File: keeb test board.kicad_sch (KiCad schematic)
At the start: 15 parts, among them SW12 SW_Push, SW14 SW_Push, SW15 SW_Push, SW3 SW_Push, SW6 SW_Push, SW9 SW_Push, U1 BluePill_V1.1

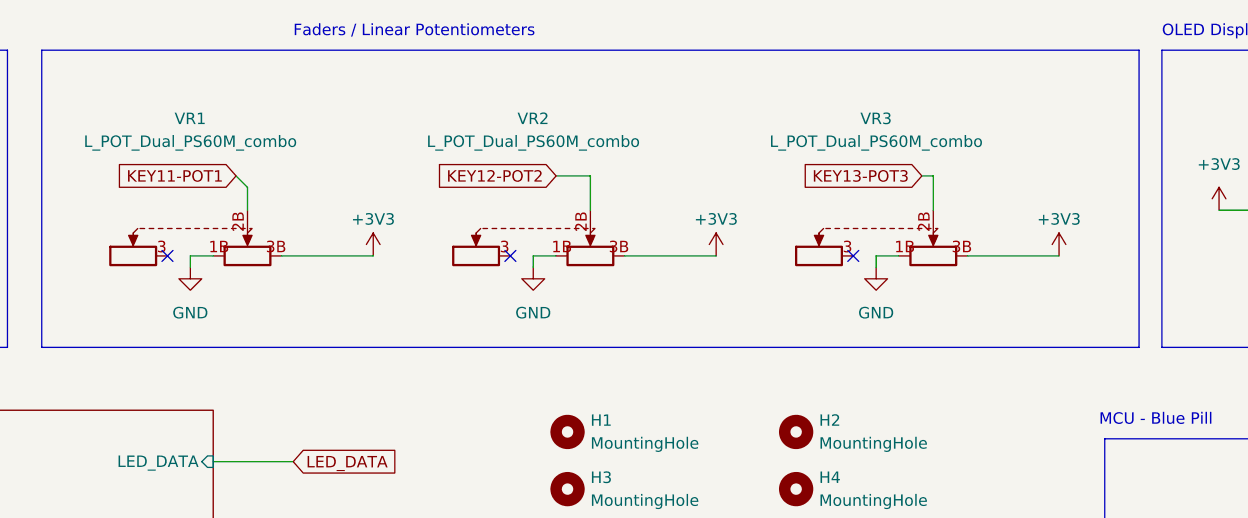
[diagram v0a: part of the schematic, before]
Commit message: LED pins fixed, lots of rerouting
Corrected LED and routed accordingly. Lots of other misc, changes to improve routing.
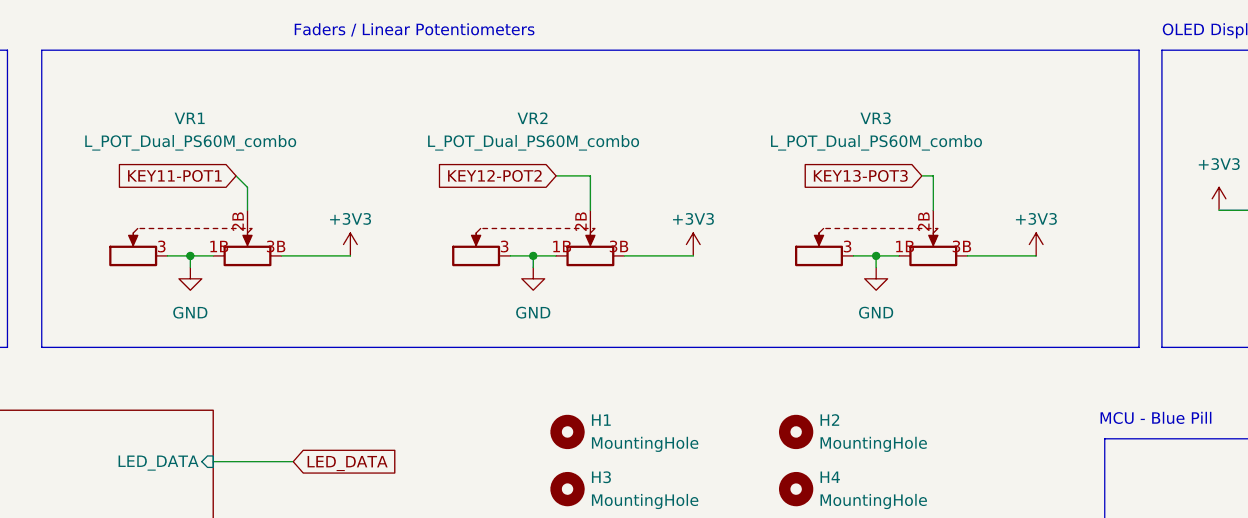
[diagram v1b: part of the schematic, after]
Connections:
- net GND: now also VR1.3, VR2.3, VR3.3
- no-connect marks 12 -> 9
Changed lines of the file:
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@@
     (rev "v${revision}")
   )
+  (junction (at 144.78 45.72) (diameter 0) (color 0 0 0 0)
+  )
   (junction (at 209.55 78.74) (diameter 0) (color 0 0 0 0)
   )
+  (junction (at 68.58 45.72) (diameter 0) (color 0 0 0 0)
+  )
   (junction (at 204.47 142.24) (diameter 0) (color 0 0 0 0)
   )
   (junction (at 207.01 142.24) (diameter 0) (color 0 0 0 0)
   )
+  (junction (at 106.68 45.72) (diameter 0) (color 0 0 0 0)
+  )
   (junction (at 212.09 78.74) (diameter 0) (color 0 0 0 0)
   )
   (no_connect (at 191.77 129.54))
-  (no_connect (at 142.24 45.72))
-  (no_connect (at 66.04 45.72))
   (no_connect (at 232.41 127))
   (no_connect (at 232.41 124.46))
@@
   (no_connect (at 232.41 91.44))
   (no_connect (at 207.01 83.82))
-  (no_connect (at 104.14 45.72))
   (wire (pts (xy 209.55 74.93) (xy 209.55 78.74))
     (stroke (width 0) (type default) (color 0 0 0 0))
@@
     (stroke (width 0) (type default) (color 0 0 0 0))
   )
+  (wire (pts (xy 66.04 45.72) (xy 68.58 45.72))
+    (stroke (width 0) (type default) (color 0 0 0 0))
+  )
   (polyline (pts (xy 36.83 35.56) (xy 38.1 35.56))
     (stroke (width 0) (type solid) (color 72 72 72 1))
@@
     (stroke (width 0) (type default) (color 0 0 0 0))
   )
-  (wire (pts (xy 78.74 45.72) (xy 88.9 45.72))
+  (wire (pts (xy 78.74 45.72) (xy 86.36 45.72))
     (stroke (width 0) (type default) (color 0 0 0 0))
   )
@@
     (stroke (width 0) (type solid) (color 0 194 0 1))
   )
+  (wire (pts (xy 142.24 45.72) (xy 144.78 45.72))
+    (stroke (width 0) (type default) (color 0 0 0 0))
+  )
   (polyline (pts (xy 27.94 33.02) (xy 31.75 33.02))
     (stroke (width 0) (type solid) (color 0 0 0 1))
@@
     (stroke (width 0) (type default) (color 0 0 0 0))
   )
-  (wire (pts (xy 116.84 45.72) (xy 127 45.72))
+  (wire (pts (xy 116.84 45.72) (xy 124.46 45.72))
     (stroke (width 0) (type default) (color 0 0 0 0))
   )
@@
     (stroke (width 0) (type default) (color 0 0 0 0))
   )
-  (wire (pts (xy 154.94 45.72) (xy 165.1 45.72))
+  (wire (pts (xy 154.94 45.72) (xy 162.56 45.72))
     (stroke (width 0) (type default) (color 0 0 0 0))
   )
@@
   (polyline (pts (xy 43.18 34.29) (xy 39.37 34.29))
     (stroke (width 0) (type solid) (color 0 0 0 1))
+  )
+  (wire (pts (xy 104.14 45.72) (xy 106.68 45.72))
+    (stroke (width 0) (type default) (color 0 0 0 0))
   )
   (wire (pts (xy 38.1 100.33) (xy 39.37 100.33))
@@
     (pin "1")
   )
-  (symbol (lib_id "power:+3V3") (at 165.1 45.72 0) (mirror y) (unit 1)
+  (symbol (lib_id "power:+3V3") (at 162.56 45.72 0) (mirror y) (unit 1)
     (in_bom yes) (on_board yes)
-    (property "Reference" "#PWR023" (id 0) (at 165.1 49.53 0)
-      (effects (font (size 1.27 1.27)) hide)
-    )
-    (property "Value" "+3V3" (id 1) (at 165.1 41.656 0))
-    (property "Footprint" "" (id 2) (at 165.1 45.72 0)
-      (effects (font (size 1.27 1.27)) hide)
-    )
-    (property "Datasheet" "" (id 3) (at 165.1 45.72 0)
+    (property "Reference" "#PWR023" (id 0) (at 162.56 49.53 0)
+      (effects (font (size 1.27 1.27)) hide)
+    )
+    (property "Value" "+3V3" (id 1) (at 162.56 41.656 0))
+    (property "Footprint" "" (id 2) (at 162.56 45.72 0)
+      (effects (font (size 1.27 1.27)) hide)
+    )
+    (property "Datasheet" "" (id 3) (at 162.56 45.72 0)
       (effects (font (size 1.27 1.27)) hide)
     )
@@
     (pin "1")
   )
-  (symbol (lib_id "power:+3V3") (at 127 45.72 0) (mirror y) (unit 1)
+  (symbol (lib_id "power:+3V3") (at 124.46 45.72 0) (mirror y) (unit 1)
     (in_bom yes) (on_board yes)
-    (property "Reference" "#PWR022" (id 0) (at 127 49.53 0)
-      (effects (font (size 1.27 1.27)) hide)
-    )
-    (property "Value" "+3V3" (id 1) (at 127 41.656 0))
-    (property "Footprint" "" (id 2) (at 127 45.72 0)
-      (effects (font (size 1.27 1.27)) hide)
-    )
-    (property "Datasheet" "" (id 3) (at 127 45.72 0)
+    (property "Reference" "#PWR022" (id 0) (at 124.46 49.53 0)
+      (effects (font (size 1.27 1.27)) hide)
+    )
+    (property "Value" "+3V3" (id 1) (at 124.46 41.656 0))
+    (property "Footprint" "" (id 2) (at 124.46 45.72 0)
+      (effects (font (size 1.27 1.27)) hide)
+    )
+    (property "Datasheet" "" (id 3) (at 124.46 45.72 0)
       (effects (font (size 1.27 1.27)) hide)
     )
@@
     )
   )
-  (symbol (lib_id "power:+3V3") (at 88.9 45.72 0) (mirror y) (unit 1)
+  (symbol (lib_id "power:+3V3") (at 86.36 45.72 0) (mirror y) (unit 1)
     (in_bom yes) (on_board yes)
-    (property "Reference" "#PWR0111" (id 0) (at 88.9 49.53 0)
-      (effects (font (size 1.27 1.27)) hide)
-    )
-    (property "Value" "+3V3" (id 1) (at 88.9 41.656 0))
-    (property "Footprint" "" (id 2) (at 88.9 45.72 0)
-      (effects (font (size 1.27 1.27)) hide)
-    )
-    (property "Datasheet" "" (id 3) (at 88.9 45.72 0)
-      (effects (font (size 1.27 1.27)) hide)
-    )
+    (property "Reference" "#PWR0111" (id 0) (at 86.36 49.53 0)
+      (effects (font (size 1.27 1.27)) hide)
+    )
+    (property "Value" "+3V3" (id 1) (at 86.36 41.656 0))
+    (property "Footprint" "" (id 2) (at 86.36 45.72 0)
+      (effects (font (size 1.27 1.27)) hide)
+    )
+    (property "Datasheet" "" (id 3) (at 86.36 45.72 0)
+      (effects (font (size 1.27 1.27)) hide)
+    )
